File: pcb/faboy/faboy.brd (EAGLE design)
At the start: 54.3 x 85.1 mm, 29 parts, among them Y1 16MHZ

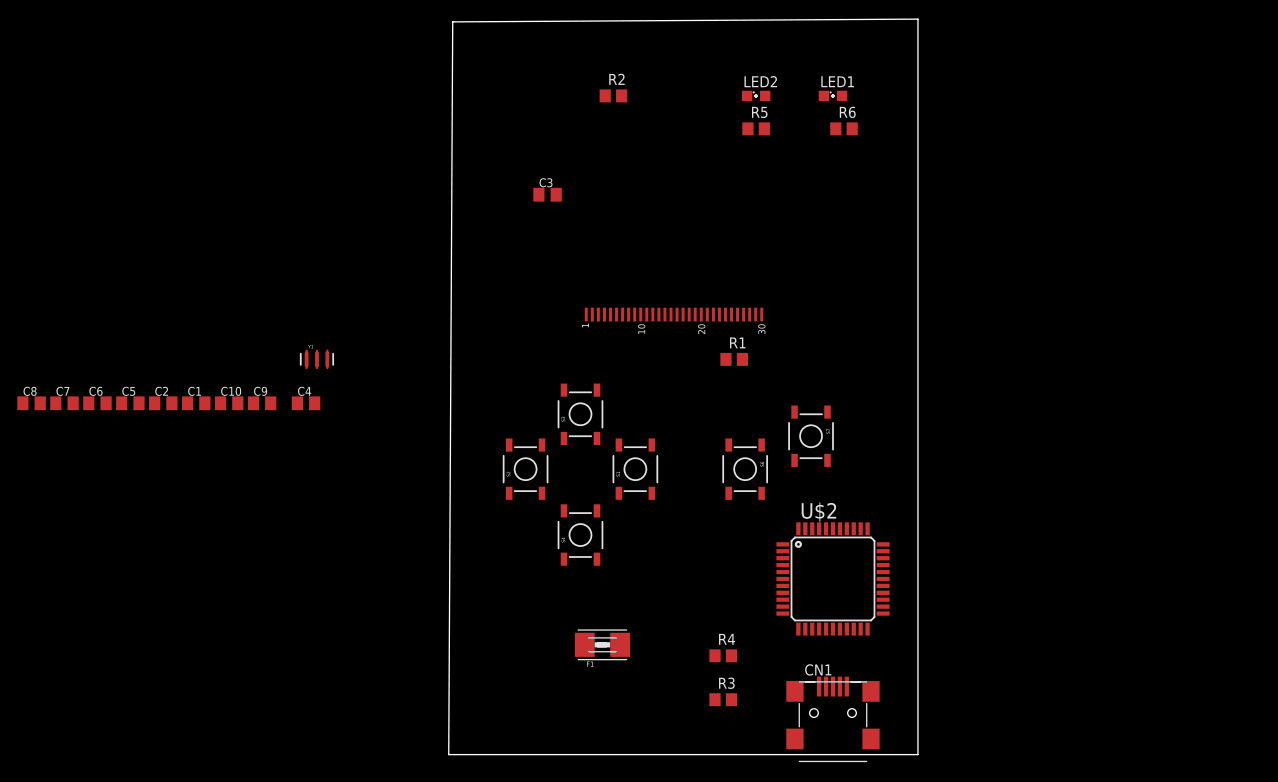
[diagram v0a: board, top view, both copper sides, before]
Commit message: schematics > dcdc, switch and battery / pcb > round courner
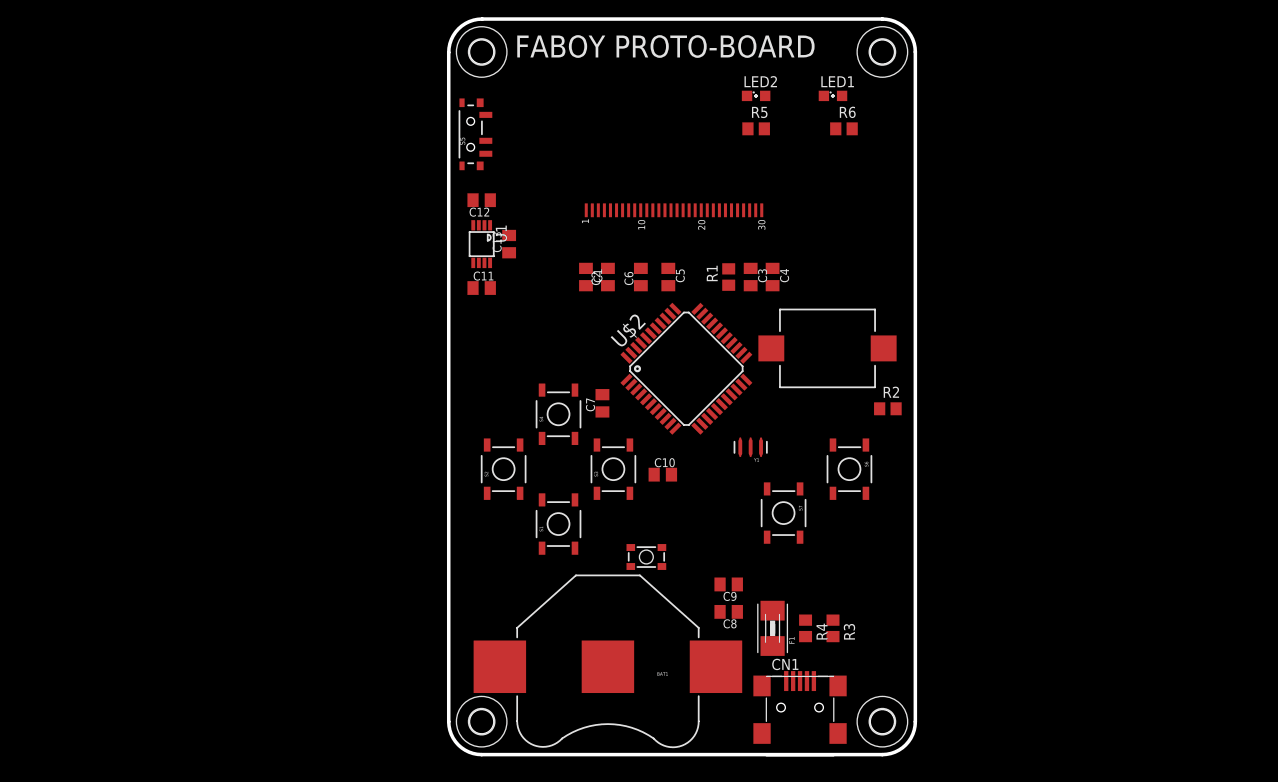
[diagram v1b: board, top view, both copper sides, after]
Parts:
- added BAT1: (no value), SparkFun-Electromechanical:BATTCON_20MM
- added C11, C12, C13: 1uF, resistor:C0805K
- added S5: (no value), SparkFun-Electromechanical:SWITCH-SPST-SMD-A
- added S8: SWITCH-MOMENTARY-2SMD-3, SparkFun-Electromechanical:TACTILE_SWITCH_SMD-3
- added SG1: BUZZERSMD3, SparkFun-Electromechanical:BUZZER-CMT1102
- added U$3, U$4, U$5, U$6: (no value), holes:2,8
- added U1: MAX1595UMAX, maxim:UMAX8
- moved C8 84.2 mm to (32.4, 16.5), turned to 180 degrees
- moved C6 64.5 mm to (22.2, 55.2), turned to 90 degrees
- moved C5 63.9 mm to (25.4, 55.2), turned to 270 degrees
- moved C7 62.2 mm to (17.8, 40.6), turned to 90 degrees
- moved C9 57.9 mm to (32.4, 19.7), turned to 180 degrees
- moved C4 55.9 mm to (37.5, 55.2), turned to 270 degrees
- moved C2 53.5 mm to (18.4, 55.2), turned to 90 degrees
- moved Y1 51.2 mm to (34.9, 35.6), turned to 180 degrees
- moved C10 50.8 mm to (24.8, 32.4)
- moved R2 48.1 mm to (50.8, 40.0)
- moved C1 47.4 mm to (15.9, 55.2), turned to 270 degrees
- moved U$2 29.6 mm to (27.5, 44.6), turned to 45 degrees
- moved C3 25.4 mm to (34.9, 55.2), turned to 270 degrees
- moved F1 19.8 mm to (37.5, 14.6), turned to 90 degrees
- moved R3 15.1 mm to (44.5, 14.6), turned to 270 degrees
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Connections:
- net N$10 renamed DOWN
- net N$15 renamed LEFT
- net N$16 renamed RIGHT
- net N$17 renamed UP
- net N$18 renamed A
- net N$19 renamed B
- new net -: BAT1.2
- new net N$10: C12.1, S5.1, U1.2, U1.3
- new net N$15: C11.1, U1.6
- new net N$16: C11.2, U1.7
- net GND: now also C12.2, C13.2, C5.2, C6.2, S8.1, U1.4, U1.5
- net N$6: now also S8.4
- net VCC: now also C13.1, C5.1, C6.1, U1.1, U1.8
- net VIN: now also BAT1.1, S5.2
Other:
- board size 54.3 x 85.1 mm -> 54 x 85.1 mm
- board text added: "FABOY PROTO-BOARD"

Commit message: schematics > rgb led / pcb > via size route
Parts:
- added C14, C15, C16: 4.7uF, resistor:C0805K
- added J1: (no value), SparkFun-Connectors:2X3_SMD
- added J2: (no value), SparkFun-Connectors:1X06-SMD-FEMALE-V2
- added LED3: (no value), led:SML0805
- added LED6: GM5WA94310A, led:GM5WA94310A
- added R10, R11, R9: 330, resistor:R0805
- added R7: 390k, resistor:R0805
- added R8: 470, resistor:R0805
- added SJ1: (no value), jumper:SJ
- added SJ2: (no value), jumper:SJ_2
- added U2: MCP73831, SparkFun-PowerIC:SOT23-5
- moved U$3 83.5 mm to (81.3, 50.2), turned to 270 degrees
- moved U$4 83.5 mm to (81.3, 3.81), turned to 270 degrees
- moved S5 72.1 mm to (71.8, 51.4), turned to 0 degrees
- moved C12 61.9 mm to (64.1, 50.2), turned to 90 degrees
- moved U1 56.0 mm to (59.1, 50.2), turned to 90 degrees
- moved S8 54.4 mm to (74.0, 4.34), turned to 90 degrees
- moved C13 53.4 mm to (59.1, 47.0), turned to 0 degrees
- moved CN1 51.2 mm to (4.45, 40.6), turned to 270 degrees
- moved U$1 50.9 mm to (63.0, 27.9), turned to 270 degrees
- moved C11 50.3 mm to (54.0, 50.2), turned to 270 degrees
- moved R6 47.6 mm to (13.3, 37.5), turned to 180 degrees
- moved LED1 47.0 mm to (17.8, 37.5)
- moved U$5 46.4 mm to (3.81, 50.2), turned to 270 degrees
- moved U$6 46.4 mm to (3.81, 3.81), turned to 270 degrees
- moved C1 42.9 mm to (55.2, 38.1), turned to 180 degrees
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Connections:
- removed net -: BAT1.2
- removed net CLK: U$1.18, U$2.9
- new net N$17: R8.1, U2.1
- new net N$18: LED3.C, R8.2
- new net N$19: R7.2, U2.5
- new net N$20: C16.2, U$2.31
- new net N$21: C16.1, SG1.1
- new net N$26: SG1.2, SJ2.2
- new net N$27: SJ2.3, U$2.32
- new net N$28: R10.2, U$2.30
- new net N$29: R11.2, U$2.12
- new net N$30: LED6.5, R11.1
- new net N$31: LED6.4, R10.1
- new net N$32: LED6.6, R9.1
- new net RST: J2.2, R2.1, S8.4, U$2.13
- new net SCLK: J2.3, U$1.18, U$2.9
- new net VBAT: BAT1.1, C15.1, U2.3
- net CS: now also U$2.26
- net DC: now also U$2.25
- net GND: now also BAT1.2, C14.2, C15.2, J2.1, R7.1, SJ2.1, U2.2
- net MISO: now also J2.4
- net MOSI: now also J2.5
- net N$10: now also SJ1.1
- net N$6: now also R9.2, U$2.29; no longer R2.1, S8.4, U$2.13
- net OLED_RST: now also U$2.27
- net VCC: now also J2.6, LED6.1, LED6.2, LED6.3, SJ1.2
- net VIN: now also C14.1, LED3.A, U2.4; no longer BAT1.1, S5.2
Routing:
- net GND: track 0.00 -> 64.4 mm, vias 0 -> 36
- net MISO: track 0.00 -> 48.9 mm, vias 0 -> 1
- net RST: track 0.00 -> 48.7 mm, vias 0 -> 1
- net MOSI: track 0.00 -> 48.6 mm, vias 0 -> 3
- net N$29: track 0.00 -> 44.0 mm, vias 0 -> 2
- net DOWN: track 0.00 -> 42.7 mm, vias 0 -> 2
- net N$22: track 0.00 -> 42.5 mm, vias 0 -> 2
- net N$24: track 0.00 -> 40.3 mm, vias 0 -> 2
- net LEFT: track 0.00 -> 34.3 mm
- net A: track 0.00 -> 33.6 mm, vias 0 -> 2
- net D-: track 0.00 -> 32.2 mm
- net D+: track 0.00 -> 30.8 mm
- net CS: track 0.00 -> 30.2 mm, vias 0 -> 2
- net DC: track 0.00 -> 29.6 mm, vias 0 -> 2
- net B: track 0.00 -> 27.2 mm
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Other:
- board size 54 x 85.1 mm -> 85.1 x 54 mm

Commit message: pcb > start to re-arange the pin
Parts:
- removed J1: (no value), SparkFun-Connectors:2X3_SMD
- moved C7 0.90 mm to (38.1, 32.4)
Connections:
- removed net N$22: R5.2, U$2.8
- removed net N$24: R6.2, U$2.22
- new net LED_RX: R6.2, U$2.8
- new net LED_TX: R5.2, U$2.1
- net A: no longer U$2.1
- net B: no longer U$2.28
- net DOWN: no longer U$2.36
- net LEFT: no longer U$2.37
- net RIGHT: no longer U$2.38
- net UP: no longer U$2.39
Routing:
- net DOWN: track 42.7 -> 0.00 mm, vias 2 -> 0
- net N$22: track 42.5 -> 0.00 mm, vias 2 -> 0
- net N$24: track 40.3 -> 0.00 mm, vias 2 -> 0
- net LED_TX: track 0.00 -> 37.7 mm, vias 0 -> 2
- net LED_RX: track 0.00 -> 35.0 mm, vias 0 -> 2
- net LEFT: track 34.3 -> 0.00 mm
- net A: track 33.6 -> 0.00 mm, vias 2 -> 0
- net B: track 27.2 -> 0.00 mm
- net RIGHT: track 21.6 -> 0.00 mm, vias 2 -> 0
- net UP: track 19.9 -> 0.00 mm
- net GND: track 64.4 -> 62.5 mm, vias 36 -> 34

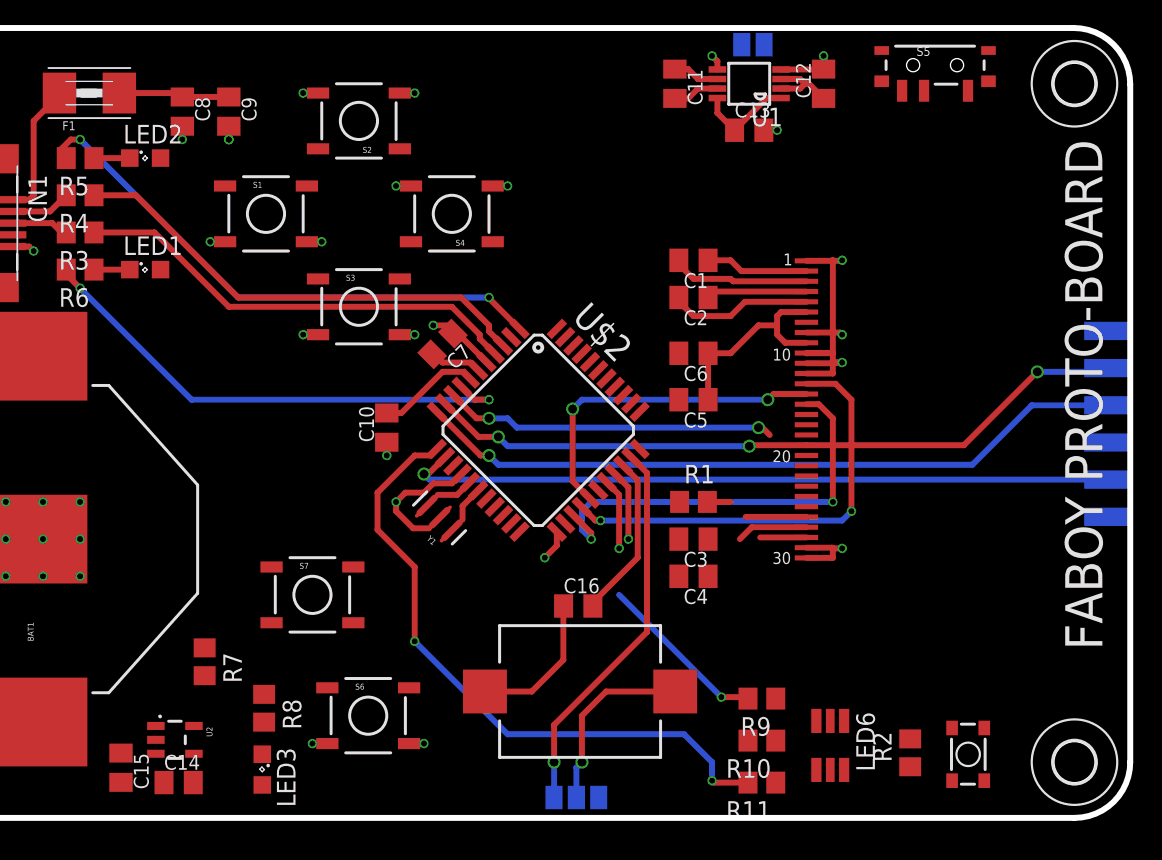
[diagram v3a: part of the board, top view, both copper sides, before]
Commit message: pcb > route oled, a and b pushbutton / change via size to 0.4mm / add QR code on layer 200 and 2001
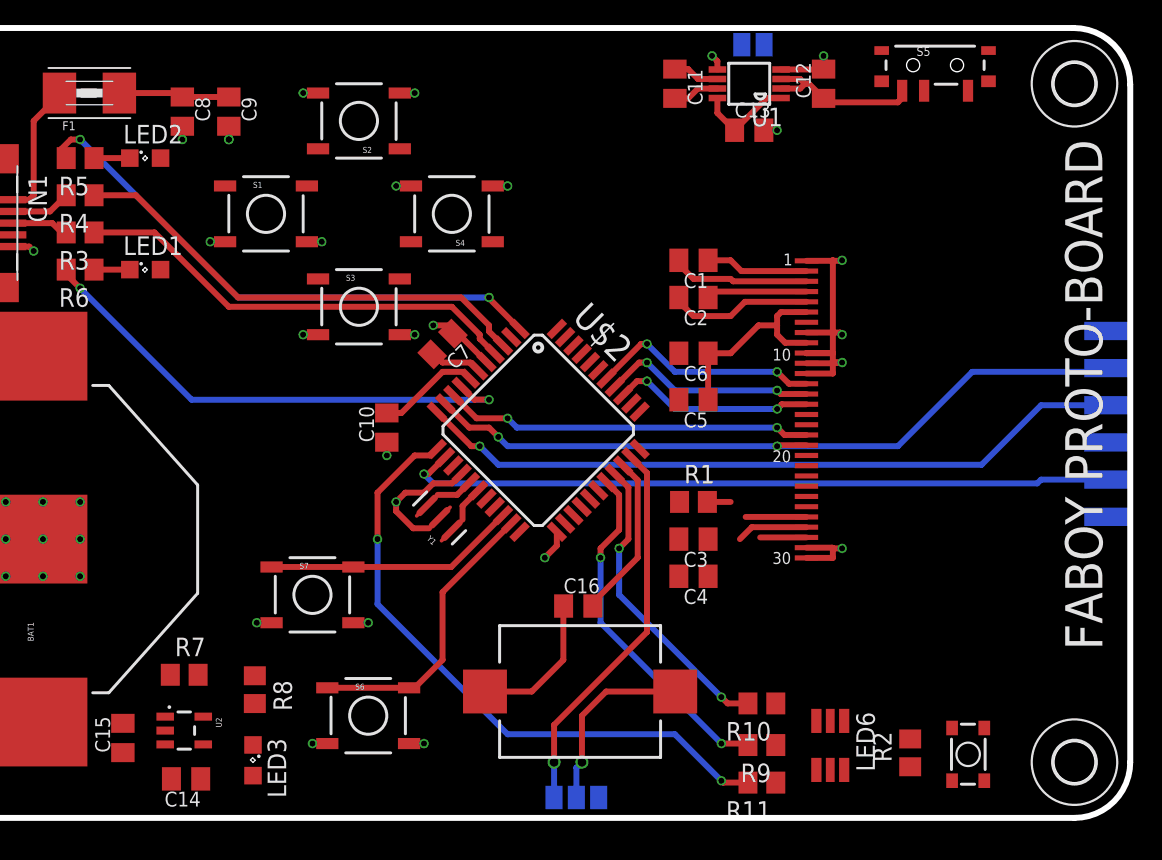
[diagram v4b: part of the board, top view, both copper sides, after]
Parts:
- moved R9 3.17 mm to (59.9, 4.98)
- moved R10 2.54 mm to (59.9, 7.82)
- moved C15 2.04 mm to (16.3, 5.46), turned to 90 degrees
- moved R7 1.66 mm to (20.4, 9.78), turned to 0 degrees
- moved R8 1.42 mm to (25.3, 8.76)
- moved U2 0.90 mm to (20.4, 5.97)
- moved LED3 0.90 mm to (25.1, 3.94)
- moved C14 0.57 mm to (20.6, 2.67), turned to 180 degrees
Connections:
- net A: now also U$2.20
- net B: now also U$2.21
- net CS: now also U$2.38; no longer U$2.26
- net DC: now also U$2.36; no longer U$2.25
- net OLED_RST: now also U$2.37; no longer U$2.27
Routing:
- net B: track 0.00 -> 19.9 mm
- net A: track 0.00 -> 17.3 mm
- net N$28: track 4.85 -> 20.8 mm, vias 1 -> 2
- net DC: track 29.6 -> 13.9 mm
- net CS: track 30.2 -> 15.8 mm
- net OLED_RST: track 23.0 -> 14.7 mm
- net N$6: track 16.6 -> 24.0 mm
- net N$10: track 5.22 -> 11.3 mm
- net SCLK: track 22.7 -> 25.3 mm
- net GND: track 62.5 -> 64.6 mm, vias 34 -> 36
- net MOSI: track 48.6 -> 50.6 mm, vias 3 -> 2
- net N$29: track 44.0 -> 43.3 mm
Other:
- board text added: "/home/louis/eagle/faboy/pcb/qrcode_github.bmp"
- board text added: "/home/louis/eagle/faboy/pcb/qrcode_id.bmp"

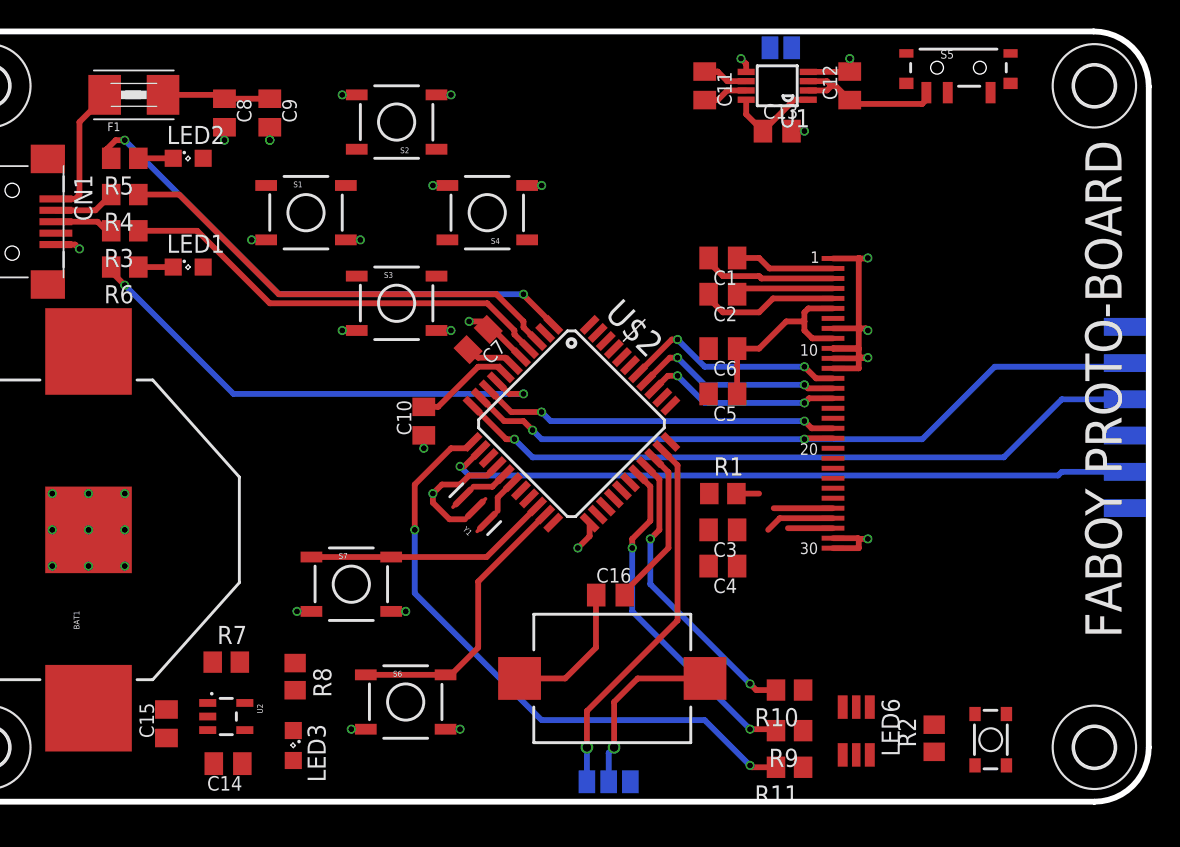
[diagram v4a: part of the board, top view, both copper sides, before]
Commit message: schematics > power path / pcb > only for 0.96 display
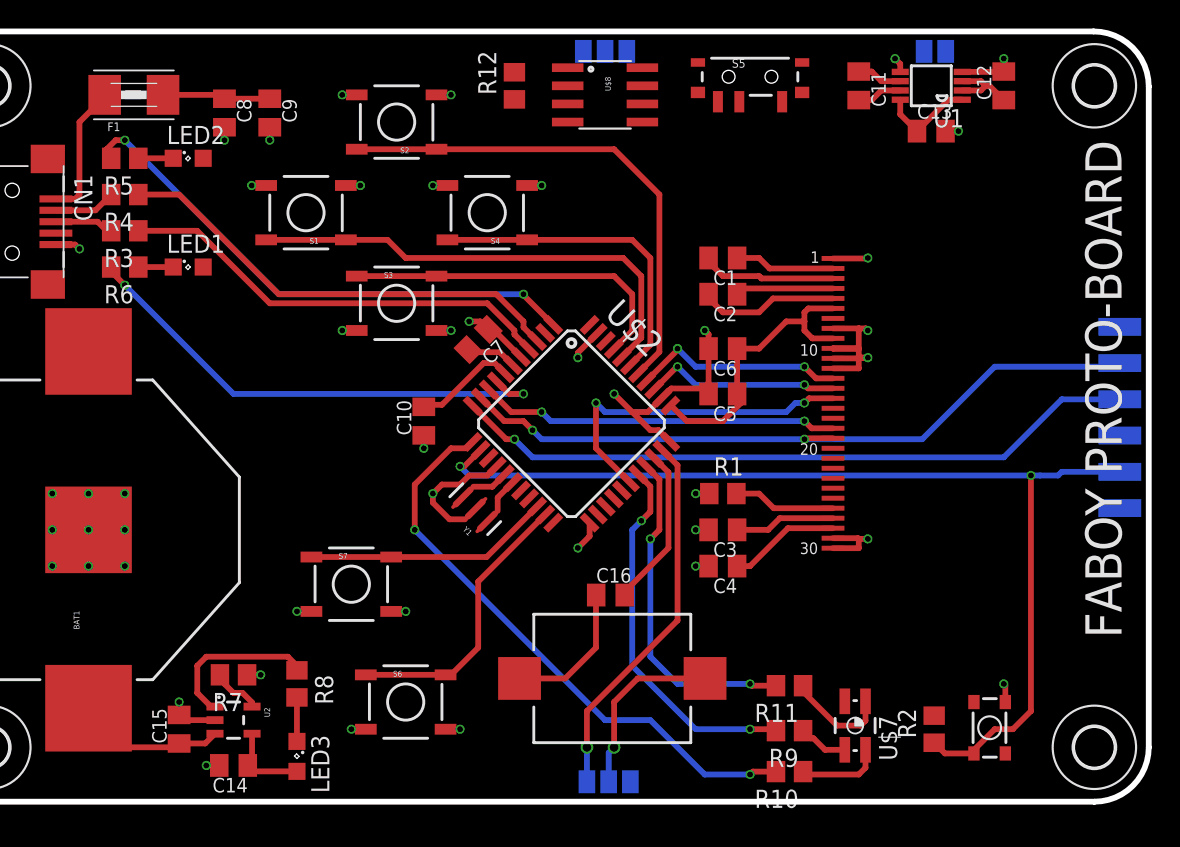
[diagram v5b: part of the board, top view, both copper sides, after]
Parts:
- removed LED6: GM5WA94310A, led:GM5WA94310A
- added R12: 10k, resistor:R0805
- added SJ3: (no value), jumper:SJ_2
- added U$7: LED-RGB-P-LCC-4, SparkFun-LED:P-LCC-4-3
- added U$8: SI4833BDY, SparkFun-DiscreteSemi:SO08
- moved S5 14.6 mm to (57.1, 50.8)
- moved SJ1 10.8 mm to (70.1, 52.6)
- moved C12 10.8 mm to (74.9, 50.2)
- moved C11 10.8 mm to (64.8, 50.2)
- moved C13 10.8 mm to (69.8, 47.0)
- moved U1 10.8 mm to (69.8, 50.2)
- moved R10 5.71 mm to (59.9, 2.11)
- moved R11 5.71 mm to (59.9, 8.13)
- moved R7 1.02 mm to (21.0, 8.89), turned to 180 degrees
- moved C15 0.97 mm to (17.1, 5.08)
- moved S8 0.84 mm to (73.9, 5.18), turned to 270 degrees
- moved LED3 0.80 mm to (25.4, 3.17)
- moved R2 0.63 mm to (70.1, 5.08)
- moved U2 0.57 mm to (21.0, 5.71)
- moved R8 0.52 mm to (25.4, 8.26)
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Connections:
- net N$6 renamed BLUE
- removed net N$29: R11.2, U$2.12
- removed net N$30: LED6.5, R11.1
- removed net N$31: LED6.4, R10.1
- removed net N$32: LED6.6, R9.1
- new net GREEN: R10.2, U$2.12
- new net N$22: R10.1, U$7.4
- new net N$24: R9.1, U$7.3
- new net N$6: R11.1, U$7.1
- new net RED: R11.2, U$2.30
- net CS: now also U$2.37; no longer U$2.38
- net DC: now also U$2.28; no longer U$2.36
- net DOWN: now also U$2.40
- net GND: now also R12.1, U$2.33
- net LEFT: now also U$2.38
- net N$10: now also S5.3; no longer S5.1
- net N$28: now also S5.2, SJ3.2, U$8.3, U$8.7, U$8.8; no longer R10.2, U$2.30
- net OLED_RST: now also U$2.36; no longer U$2.37
- net RIGHT: now also U$2.41
- net UP: now also U$2.39
- net VBAT: now also SJ3.1, U$8.5, U$8.6
- net VCC: now also U$7.2; no longer LED6.1, LED6.2, LED6.3
- net VIN: now also R12.2, SJ3.3, U$8.1, U$8.2, U$8.4
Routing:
- net N$29: track 43.3 -> 0.00 mm, vias 2 -> 0
- net GREEN: track 0.00 -> 41.0 mm, vias 0 -> 2
- net LEFT: track 0.00 -> 35.7 mm
- net DOWN: track 0.00 -> 33.6 mm
- net RST: track 48.9 -> 73.5 mm, vias 1 -> 2
- net RIGHT: track 0.00 -> 24.2 mm
- net RED: track 0.00 -> 23.6 mm, vias 0 -> 2
- net UP: track 0.00 -> 22.9 mm
- net GND: track 64.6 -> 87.0 mm, vias 36 -> 45
- net N$28: track 20.8 -> 0.00 mm, vias 2 -> 0
- net N$17: track 0.00 -> 11.4 mm
- net VBAT: track 0.00 -> 10.5 mm
- net DC: track 13.9 -> 23.8 mm
- net N$6: track 0.00 -> 7.27 mm
- net VCC: track 21.1 -> 27.7 mm
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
